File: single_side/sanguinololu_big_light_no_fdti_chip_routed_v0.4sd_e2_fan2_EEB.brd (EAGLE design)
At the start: 74 parts, among them IC1 LM7805, IC2 ATMEGA644-20PU, P1 POLOLU-X, P2 POLOLU-Y, P3 POLOLU-Z, P4 POLOLU-E, P5 POLOLU-X, Q1 RFP30N06LE, Q2 RFP30N06LE, Q4 BD139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

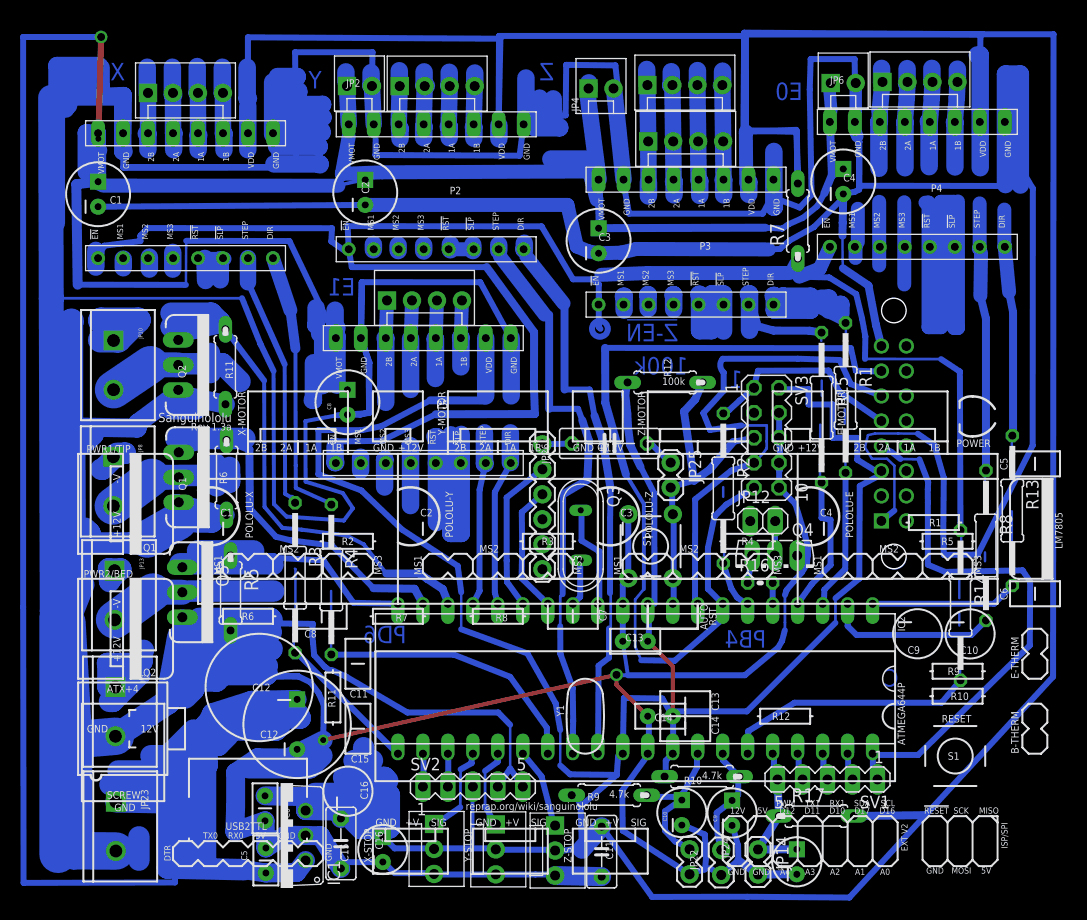
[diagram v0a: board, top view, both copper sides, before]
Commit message: beefed up the tracks and soldering pads
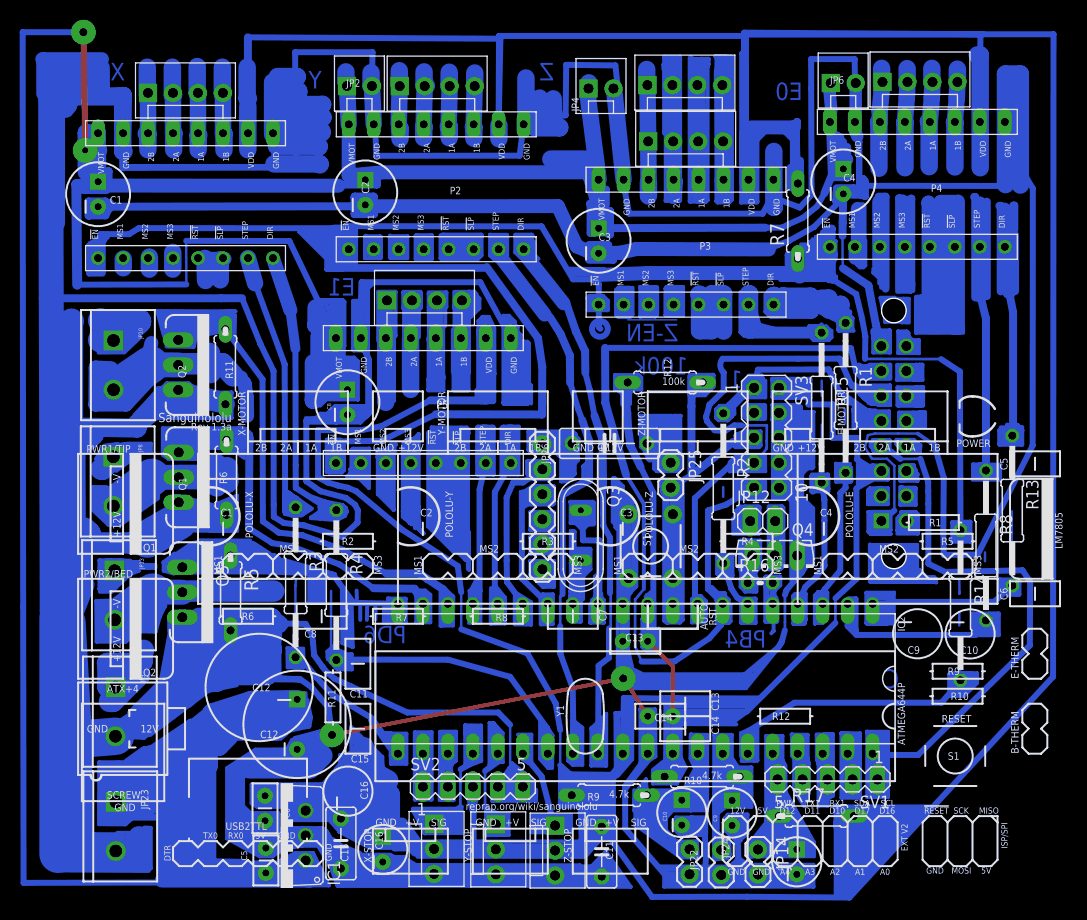
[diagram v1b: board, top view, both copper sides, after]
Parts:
- moved R4 0.76 mm to (26.8, 29.8)
- moved R3 0.47 mm to (22.6, 30.1)
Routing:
- net N$711: track 0.00 -> 129.2 mm
- net N$741: track 0.00 -> 124.7 mm
- net N$353: track 0.00 -> 62.5 mm
- net N$387: track 0.00 -> 62.2 mm
- net N$714: track 0.00 -> 60.5 mm
- net N$730: track 0.00 -> 59.5 mm
- net N$740: track 0.00 -> 57.0 mm
- net N$619: track 0.00 -> 50.6 mm
- net N$388: track 0.00 -> 49.2 mm
- net N$691: track 0.00 -> 48.3 mm
- net N$717: track 0.00 -> 47.3 mm
- net N$731: track 0.00 -> 45.7 mm
- net N$725: track 0.00 -> 44.0 mm
- net N$587: track 0.00 -> 43.1 mm
- net N$708: track 0.00 -> 43.1 mm
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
